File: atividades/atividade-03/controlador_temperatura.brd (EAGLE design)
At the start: 68.6 x 53.3 mm, 34 parts, among them Q1 BC337, Q2 BC337, Q3 BC337

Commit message: posicionamento de alguns conectores
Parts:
- moved SHIELD_ARDUINO_CB2 152.5 mm to (57.1, 2.54)
- moved SHIELD_ARDUINO_CB1 119.5 mm to (39.4, 2.54)
- moved SHIELD_ARDUINO_CT2 96.6 mm to (33.0, 50.8)
- moved SHIELD_ARDUINO_CT1 93.2 mm to (54.6, 50.8)
- moved SHIELD 86.9 mm to (50.8, 26.7), turned to 180 degrees
- moved DISPLAY 44.5 mm to (-69.8, 2.54)

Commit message: agrupando os componentes
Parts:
- moved R6 174.7 mm to (121.9, 35.6)
- moved V1 168.3 mm to (121.9, 47.0)
- moved R10 160.7 mm to (48.3, 158.8)
- moved R9 140.5 mm to (33.0, 160.0)
- moved RST 127.8 mm to (31.8, -25.4)
- moved Q3 123.8 mm to (-10.2, -22.9)
- moved R8 117.6 mm to (14.0, 158.8)
- moved BUTTONS 116.6 mm to (31.8, 146.1)
- moved BUZZ 114.6 mm to (8.89, -21.6)
- moved R11 109.6 mm to (62.2, 157.5)
- moved HTR 106.3 mm to (-88.9, 125.7)
- moved R7 105.7 mm to (-1.27, -14.0)
- moved R3 93.8 mm to (-100.3, 119.4)
- moved DS18B20 88.3 mm to (-3.81, 128.3)
- moved D1 87.7 mm to (-111.8, 132.1)
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
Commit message: buzz realinhado
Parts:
- moved RST 27.9 mm to (57.1, -36.8)
- moved R7 11.4 mm to (-11.4, -19.1), turned to 90 degrees
- moved BUZZ 7.73 mm to (1.27, -22.9), turned to 90 degrees
- moved Q3 5.08 mm to (-5.08, -22.9), turned to 90 degrees

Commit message: rst realinahdo
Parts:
- moved RST 32.5 mm to (36.8, -11.4)
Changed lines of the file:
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@@
 <attribute name="VALUE" x="30.48" y="156.845" size="1.778" layer="27" ratio="10"/>
 </element>
-<element name="RST" library="con-amp" library_urn="urn:adsk.eagle:library:127" package="10X02MTA" package3d_urn="urn:adsk.eagle:package:8081649/1" value="" x="57.15" y="-36.83" smashed="yes">
-<attribute name="NAME" x="54.5338" y="-40.0812" size="1.27" layer="25"/>
-<attribute name="POPULARITY" value="5" x="80.01" y="-127" size="1.778" layer="27" display="off"/>
-<attribute name="VALUE" x="54.6039" y="-34.6791" size="1.27" layer="27"/>
+<element name="RST" library="con-amp" library_urn="urn:adsk.eagle:library:127" package="10X02MTA" package3d_urn="urn:adsk.eagle:package:8081649/1" value="" x="36.83" y="-11.43" smashed="yes">
+<attribute name="NAME" x="34.2138" y="-14.6812" size="1.27" layer="25"/>
+<attribute name="POPULARITY" value="5" x="59.69" y="-101.6" size="1.778" layer="27" display="off"/>
+<attribute name="VALUE" x="34.2839" y="-9.2791" size="1.27" layer="27"/>
 </element>
 <element name="SHIELD" library="con-panduit" library_urn="urn:adsk.eagle:library:169" package="057-016-1" package3d_urn="urn:adsk.eagle:package:9196/1" value="SCD" x="101.6" y="25.4" smashed="yes" rot="R180">
@@
 <wire x1="43.18" y1="-2.54" x2="92.71" y2="24.13" width="0" layer="19" extent="1-1"/>
 <wire x1="40.64" y1="-2.54" x2="43.18" y2="-2.54" width="0" layer="19" extent="1-1"/>
-<wire x1="58.42" y1="-36.83" x2="43.18" y2="-2.54" width="0" layer="19" extent="1-1"/>
+<wire x1="38.1" y1="-11.43" x2="43.18" y2="-2.54" width="0" layer="19" extent="1-1"/>
 <wire x1="-5.08" y1="-21.59" x2="40.64" y2="-2.54" width="0" layer="19" extent="1-1"/>
 </signal>
@@
 <contactref element="RST" pad="2"/>
 <contactref element="SHIELD_ARDUINO_CB1" pad="1"/>
-<wire x1="33.02" y1="-2.54" x2="55.88" y2="-36.83" width="0" layer="19" extent="1-1"/>
+<wire x1="33.02" y1="-2.54" x2="35.56" y2="-11.43" width="0" layer="19" extent="1-1"/>
 </signal>
 <signal name="A0">

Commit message: power realinhado
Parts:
- moved PWR 86.2 mm to (-40.6, 22.9), flipped to the bottom
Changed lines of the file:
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@@
 <attribute name="VALUE" x="-85.0961" y="84.7009" size="1.27" layer="27"/>
 </element>
-<element name="PWR" library="con-phoenix-508" library_urn="urn:adsk.eagle:library:176" package="MKDSN1,5/2-5,08" package3d_urn="urn:adsk.eagle:package:9630/1" value="MKDSN1,5/2-5,08" x="-125.73" y="36.83" smashed="yes">
-<attribute name="NAME" x="-130.4811" y="41.275" size="1.27" layer="25"/>
-<attribute name="POPULARITY" value="14" x="-77.47" y="-7.62" size="1.778" layer="27" display="off"/>
-<attribute name="VALUE" x="-118.745" y="33.02" size="1.27" layer="27" rot="R90"/>
+<element name="PWR" library="con-phoenix-508" library_urn="urn:adsk.eagle:library:176" package="MKDSN1,5/2-5,08" package3d_urn="urn:adsk.eagle:package:9630/1" value="MKDSN1,5/2-5,08" x="-40.64" y="22.86" smashed="yes" rot="MR0">
+<attribute name="NAME" x="-35.8889" y="27.305" size="1.27" layer="26" rot="MR0"/>
+<attribute name="POPULARITY" value="14" x="-88.9" y="-21.59" size="1.778" layer="28" rot="MR0" display="off"/>
+<attribute name="VALUE" x="-47.625" y="19.05" size="1.27" layer="28" rot="MR90"/>
 </element>
 <element name="Q1" library="transistor-npn" library_urn="urn:adsk.eagle:library:398" package="TO92" package3d_urn="urn:adsk.eagle:package:28523/2" value="BC337" x="-114.3" y="123.19" smashed="yes">
@@
 <wire x1="-113.03" y1="123.19" x2="-76.2" y2="87.63" width="0" layer="19" extent="1-1"/>
 <wire x1="-105.41" y1="139.7" x2="-113.03" y2="123.19" width="0" layer="19" extent="1-1"/>
-<wire x1="-123.2111" y1="36.855" x2="-76.2" y2="87.63" width="0" layer="19" extent="1-1"/>
-<wire x1="48.26" y1="55.88" x2="-1.2911" y2="128.295" width="0" layer="19" extent="1-1"/>
-<wire x1="92.71" y1="24.13" x2="48.26" y2="55.88" width="0" layer="19" extent="1-1"/>
+<wire x1="-43.1589" y1="22.885" x2="-76.2" y2="87.63" width="0" layer="19" extent="1-1"/>
+<wire x1="-5.08" y1="-21.59" x2="-43.1589" y2="22.885" width="0" layer="19" extent="1-1"/>
+<wire x1="38.1" y1="-11.43" x2="-5.08" y2="-21.59" width="0" layer="19" extent="1-1"/>
+<wire x1="40.64" y1="-2.54" x2="38.1" y2="-11.43" width="0" layer="19" extent="1-1"/>
+<wire x1="43.18" y1="-2.54" x2="40.64" y2="-2.54" width="0" layer="19" extent="1-1"/>
+<wire x1="92.71" y1="24.13" x2="43.18" y2="-2.54" width="0" layer="19" extent="1-1"/>
 <wire x1="100.33" y1="24.13" x2="92.71" y2="24.13" width="0" layer="19" extent="1-1"/>
 <wire x1="102.87" y1="24.13" x2="100.33" y2="24.13" width="0" layer="19" extent="1-1"/>
@@
 <wire x1="110.49" y1="26.67" x2="105.41" y2="26.67" width="0" layer="19" extent="1-1"/>
 <wire x1="119.38" y1="46.99" x2="110.49" y2="26.67" width="0" layer="19" extent="1-1"/>
-<wire x1="43.18" y1="-2.54" x2="92.71" y2="24.13" width="0" layer="19" extent="1-1"/>
-<wire x1="40.64" y1="-2.54" x2="43.18" y2="-2.54" width="0" layer="19" extent="1-1"/>
-<wire x1="38.1" y1="-11.43" x2="43.18" y2="-2.54" width="0" layer="19" extent="1-1"/>
-<wire x1="-5.08" y1="-21.59" x2="40.64" y2="-2.54" width="0" layer="19" extent="1-1"/>
+<wire x1="48.26" y1="55.88" x2="92.71" y2="24.13" width="0" layer="19" extent="1-1"/>
 </signal>
 <signal name="N$1">
@@
 <contactref element="BUZZ" pad="1"/>
 <contactref element="SHIELD_ARDUINO_CB1" pad="6"/>
-<wire x1="-96.52" y1="119.38" x2="1.27" y2="-21.59" width="0" layer="19" extent="1-1"/>
-<wire x1="-69.85" y1="74.93" x2="-96.52" y2="119.38" width="0" layer="19" extent="1-1"/>
-<wire x1="-116.84" y1="132.08" x2="-69.85" y2="74.93" width="0" layer="19" extent="1-1"/>
-<wire x1="45.72" y1="-2.54" x2="-116.84" y2="132.08" width="0" layer="19" extent="1-1"/>
-<wire x1="-69.85" y1="90.17" x2="-116.84" y2="132.08" width="0" layer="19" extent="1-1"/>
-<wire x1="-54.6311" y1="83.845" x2="-69.85" y2="74.93" width="0" layer="19" extent="1-1"/>
-<wire x1="-91.4611" y1="125.755" x2="-54.6311" y2="83.845" width="0" layer="19" extent="1-1"/>
-<wire x1="-128.2911" y1="36.855" x2="-54.6311" y2="83.845" width="0" layer="19" extent="1-1"/>
+<wire x1="1.27" y1="-21.59" x2="45.72" y2="-2.54" width="0" layer="19" extent="1-1"/>
+<wire x1="-38.0789" y1="22.885" x2="1.27" y2="-21.59" width="0" layer="19" extent="1-1"/>
+<wire x1="-69.85" y1="74.93" x2="-38.0789" y2="22.885" width="0" layer="19" extent="1-1"/>
+<wire x1="-69.85" y1="90.17" x2="-69.85" y2="74.93" width="0" layer="19" extent="1-1"/>
+<wire x1="-54.6311" y1="83.845" x2="-69.85" y2="90.17" width="0" layer="19" extent="1-1"/>
+<wire x1="-96.52" y1="119.38" x2="-69.85" y2="90.17" width="0" layer="19" extent="1-1"/>
+<wire x1="-91.4611" y1="125.755" x2="-96.52" y2="119.38" width="0" layer="19" extent="1-1"/>
+<wire x1="-116.84" y1="132.08" x2="-96.52" y2="119.38" width="0" layer="19" extent="1-1"/>
 </signal>
 <signal name="N$5">

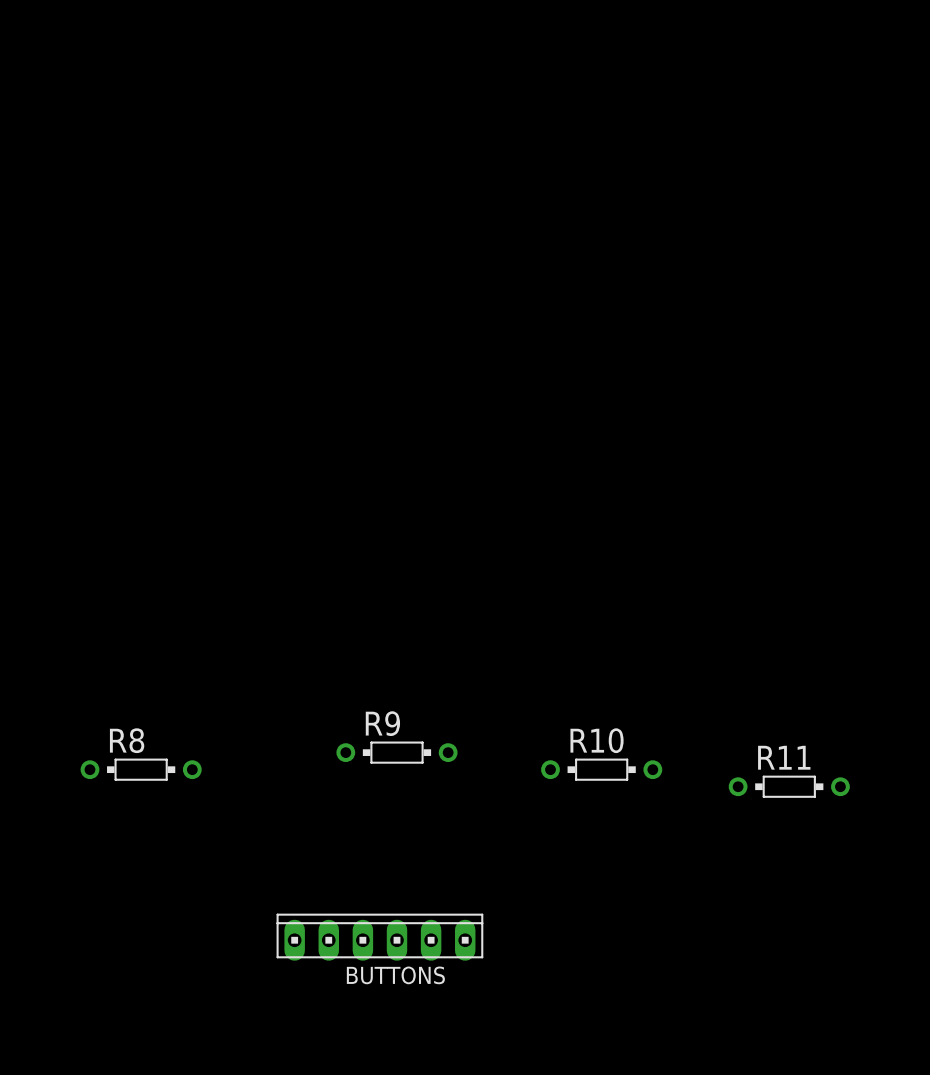
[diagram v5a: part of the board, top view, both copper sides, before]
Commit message: buttons realinhado
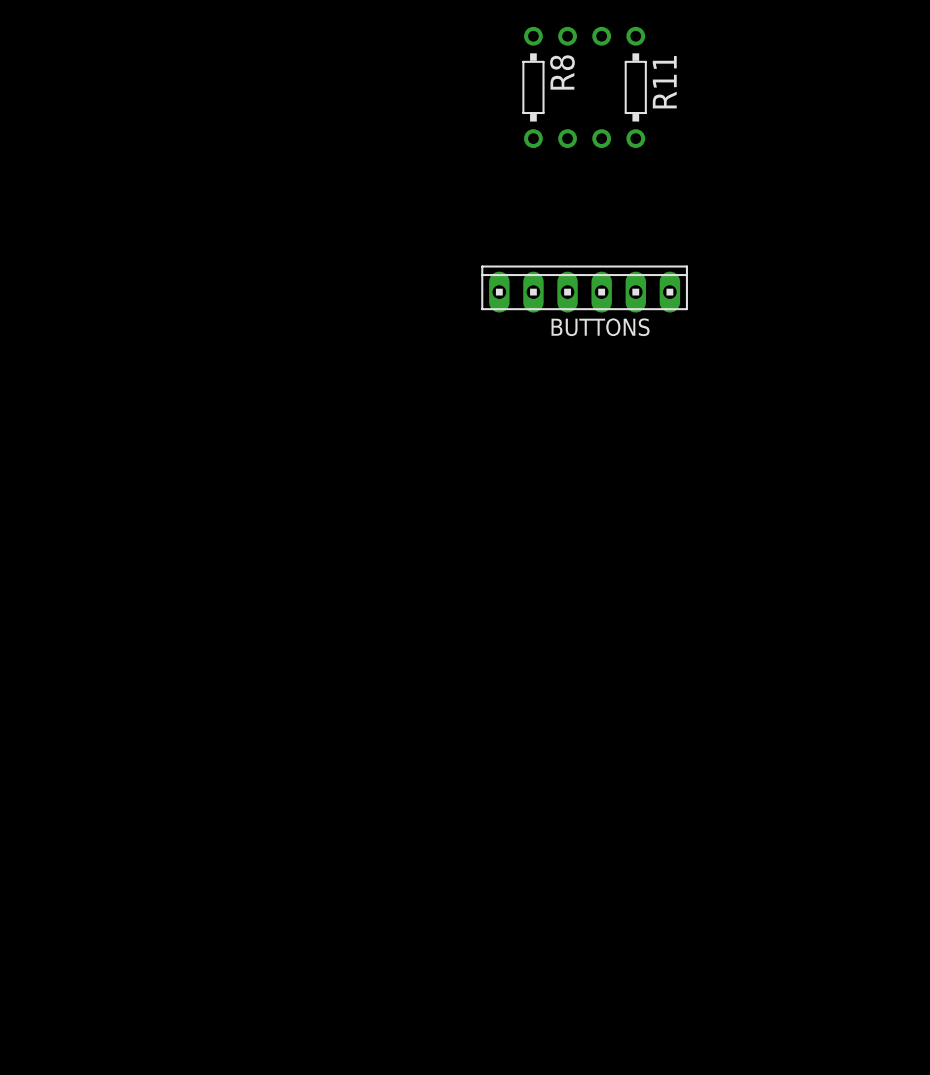
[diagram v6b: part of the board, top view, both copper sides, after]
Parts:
- moved R8 58.6 mm to (43.2, 209.6), turned to 270 degrees
- moved R11 53.3 mm to (50.8, 209.6), turned to 270 degrees
- moved R9 51.1 mm to (45.7, 209.6), flipped to the bottom, turned to 270 degrees
- moved R10 50.8 mm to (48.3, 209.6), flipped to the bottom, turned to 270 degrees
- moved BUTTONS 50.6 mm to (47.0, 194.3)

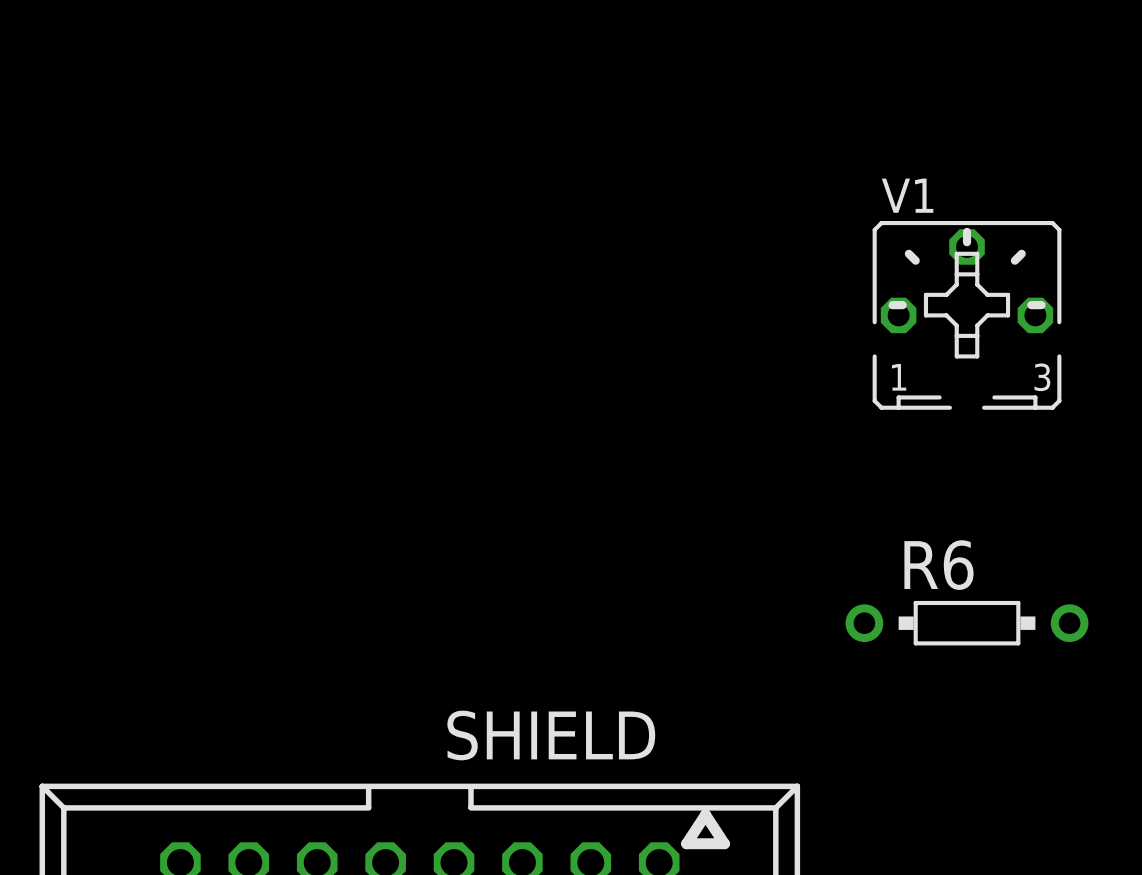
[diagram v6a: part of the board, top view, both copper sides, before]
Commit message: conector do shield_display realinhado
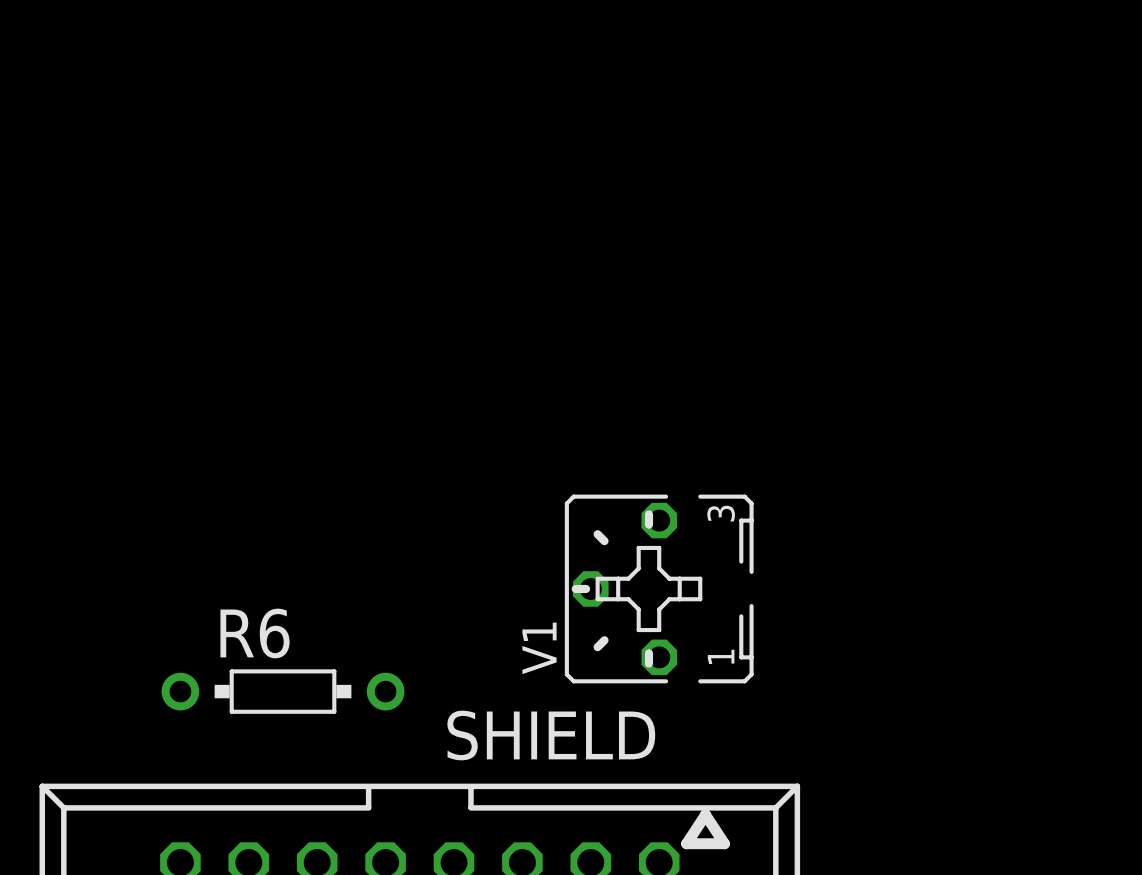
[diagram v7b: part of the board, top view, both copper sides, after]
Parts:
- moved R6 25.5 mm to (96.5, 33.0)
- moved V1 15.3 mm to (110.5, 36.8), turned to 90 degrees
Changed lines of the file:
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@@
 <attribute name="VALUE" x="-76.2" y="71.755" size="1.778" layer="27" ratio="10"/>
 </element>
-<element name="R6" library="resistor-power" library_urn="urn:adsk.eagle:library:344" package="RS1/8" package3d_urn="urn:adsk.eagle:package:25168/1" value="220" x="121.92" y="35.56" smashed="yes">
-<attribute name="MF" value="" x="170.18" y="-39.37" size="1.778" layer="27" display="off"/>
-<attribute name="MPN" value="" x="170.18" y="-39.37" size="1.778" layer="27" display="off"/>
-<attribute name="NAME" x="119.38" y="36.83" size="1.778" layer="25" ratio="10"/>
-<attribute name="OC_FARNELL" value="unknown" x="170.18" y="-39.37" size="1.778" layer="27" display="off"/>
-<attribute name="OC_NEWARK" value="unknown" x="170.18" y="-39.37" size="1.778" layer="27" display="off"/>
-<attribute name="POPULARITY" value="0" x="170.18" y="-39.37" size="1.778" layer="27" display="off"/>
-<attribute name="VALUE" x="119.38" y="32.385" size="1.778" layer="27" ratio="10"/>
+<element name="R6" library="resistor-power" library_urn="urn:adsk.eagle:library:344" package="RS1/8" package3d_urn="urn:adsk.eagle:package:25168/1" value="220" x="96.52" y="33.02" smashed="yes">
+<attribute name="MF" value="" x="144.78" y="-41.91" size="1.778" layer="27" display="off"/>
+<attribute name="MPN" value="" x="144.78" y="-41.91" size="1.778" layer="27" display="off"/>
+<attribute name="NAME" x="93.98" y="34.29" size="1.778" layer="25" ratio="10"/>
+<attribute name="OC_FARNELL" value="unknown" x="144.78" y="-41.91" size="1.778" layer="27" display="off"/>
+<attribute name="OC_NEWARK" value="unknown" x="144.78" y="-41.91" size="1.778" layer="27" display="off"/>
+<attribute name="POPULARITY" value="0" x="144.78" y="-41.91" size="1.778" layer="27" display="off"/>
+<attribute name="VALUE" x="93.98" y="29.845" size="1.778" layer="27" ratio="10"/>
 </element>
 <element name="R7" library="resistor-power" library_urn="urn:adsk.eagle:library:344" package="RS1/8" package3d_urn="urn:adsk.eagle:package:25168/1" value="470" x="-11.43" y="-19.05" smashed="yes" rot="R90">
@@
 <attribute name="VALUE" x="22.86" y="52.959" size="1.27" layer="27" ratio="10"/>
 </element>
-<element name="V1" library="pot" library_urn="urn:adsk.eagle:library:331" package="B25P" package3d_urn="urn:adsk.eagle:package:22684/1" value="10K" x="121.92" y="46.99" smashed="yes">
-<attribute name="NAME" x="118.745" y="50.8" size="1.27" layer="25" ratio="10"/>
-<attribute name="POPULARITY" value="7" x="167.64" y="-15.24" size="1.778" layer="27" display="off"/>
-<attribute name="VALUE" x="118.7704" y="41.91" size="1.27" layer="27" ratio="10"/>
+<element name="V1" library="pot" library_urn="urn:adsk.eagle:library:331" package="B25P" package3d_urn="urn:adsk.eagle:package:22684/1" value="10K" x="110.49" y="36.83" smashed="yes" rot="R90">
+<attribute name="NAME" x="106.68" y="33.655" size="1.27" layer="25" ratio="10" rot="R90"/>
+<attribute name="POPULARITY" value="7" x="172.72" y="82.55" size="1.778" layer="27" rot="R90" display="off"/>
+<attribute name="VALUE" x="115.57" y="33.6804" size="1.27" layer="27" ratio="10" rot="R90"/>
 </element>
 </elements>
@@
 <wire x1="100.33" y1="26.67" x2="100.33" y2="24.13" width="0" layer="19" extent="1-1"/>
 <wire x1="110.49" y1="26.67" x2="105.41" y2="26.67" width="0" layer="19" extent="1-1"/>
-<wire x1="119.38" y1="46.99" x2="110.49" y2="26.67" width="0" layer="19" extent="1-1"/>
+<wire x1="110.49" y1="34.29" x2="110.49" y2="26.67" width="0" layer="19" extent="1-1"/>
 <wire x1="48.26" y1="55.88" x2="92.71" y2="24.13" width="0" layer="19" extent="1-1"/>
 </signal>
@@
 <contactref element="SHIELD_ARDUINO_CB1" pad="3"/>
 <contactref element="SHIELD" pad="2"/>
-<wire x1="43.18" y1="213.36" x2="45.72" y2="213.36" width="0" layer="19" extent="1-1"/>
+<wire x1="100.33" y1="33.02" x2="110.49" y2="39.37" width="0" layer="19" extent="1-1"/>
+<wire x1="110.49" y1="24.13" x2="100.33" y2="33.02" width="0" layer="19" extent="1-1"/>
+<wire x1="38.1" y1="-2.54" x2="110.49" y2="24.13" width="0" layer="19" extent="1-1"/>
+<wire x1="-10.16" y1="120.65" x2="38.1" y2="-2.54" width="0" layer="19" extent="1-1"/>
+<wire x1="-11.4511" y1="128.295" x2="-10.16" y2="120.65" width="0" layer="19" extent="1-1"/>
+<wire x1="43.18" y1="213.36" x2="-11.4511" y2="128.295" width="0" layer="19" extent="1-1"/>
+<wire x1="45.72" y1="213.36" x2="43.18" y2="213.36" width="0" layer="19" extent="1-1"/>
 <wire x1="48.26" y1="213.36" x2="45.72" y2="213.36" width="0" layer="19" extent="1-1"/>
 <wire x1="50.8" y1="213.36" x2="48.26" y2="213.36" width="0" layer="19" extent="1-1"/>
-<wire x1="-11.4511" y1="128.295" x2="43.18" y2="213.36" width="0" layer="19" extent="1-1"/>
-<wire x1="-10.16" y1="120.65" x2="-11.4511" y2="128.295" width="0" layer="19" extent="1-1"/>
-<wire x1="38.1" y1="-2.54" x2="-10.16" y2="120.65" width="0" layer="19" extent="1-1"/>
-<wire x1="110.49" y1="24.13" x2="38.1" y2="-2.54" width="0" layer="19" extent="1-1"/>
-<wire x1="125.73" y1="35.56" x2="110.49" y2="24.13" width="0" layer="19" extent="1-1"/>
-<wire x1="124.46" y1="46.99" x2="125.73" y2="35.56" width="0" layer="19" extent="1-1"/>
 </signal>
 <signal name="A5">
@@
 <contactref element="SHIELD" pad="15"/>
 <contactref element="R6" pad="1"/>
-<wire x1="118.11" y1="35.56" x2="92.71" y2="26.67" width="0" layer="19" extent="1-1"/>
+<wire x1="92.71" y1="33.02" x2="92.71" y2="26.67" width="0" layer="19" extent="1-1"/>
 </signal>
 <signal name="N$26">
 <contactref element="SHIELD" pad="3"/>
 <contactref element="V1" pad="S"/>
-<wire x1="121.92" y1="49.53" x2="107.95" y2="26.67" width="0" layer="19" extent="1-1"/>
+<wire x1="107.95" y1="26.67" x2="107.95" y2="36.83" width="0" layer="19" extent="1-1"/>
 </signal>
 </signals>

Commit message: pump realinhado
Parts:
- moved PUMP_LED 50.6 mm to (-33.0, 72.4), turned to 270 degrees
- moved D2 34.2 mm to (-47.0, 61.0), turned to 90 degrees
- moved PUMP 29.8 mm to (-33.0, 61.0), turned to 90 degrees
- moved Q2 23.2 mm to (-73.7, 64.8), flipped to the bottom, turned to 270 degrees
- moved R5 18.3 mm to (-58.4, 64.8), turned to 270 degrees
- moved R4 13.0 mm to (-77.5, 76.2), turned to 90 degrees
